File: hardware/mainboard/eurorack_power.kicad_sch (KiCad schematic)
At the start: 11 parts, among them J1 Eurorack PWR

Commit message: Add mixer circuitry
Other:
- moved on the sheet: C1, C2, C3, C4, D1, D2, D3, D4, J1, R1, R2

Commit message: Add footprints
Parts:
- C1, C2: footprint (none) -> Capacitor_SMD:CP_Elec_6.3x5.9
- C3, C4: footprint (none) -> Capacitor_SMD:C_0805_2012Metric_Pad1.18x1.45mm_HandSolder
- D1, D2: footprint (none) -> Diode_SMD:D_SOD-323F
- D3, D4: footprint (none) -> LED_SMD:LED_0805_2012Metric_Pad1.15x1.40mm_HandSolder
- J1: footprint (none) -> Connector_IDC:IDC-Header_2x05_P2.54mm_Latch6.5mm_Vertical
- R1, R2: footprint (none) -> Resistor_SMD:R_0805_2012Metric_Pad1.20x1.40mm_HandSolder

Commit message: Layout
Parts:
- J1: value Eurorack PWR -> Power Connector; footprint Connector_IDC:IDC-Header_2x05_P2.54mm_Latch6.5mm_Vertical -> Connector_IDC:IDC-Header_2x05_P2.54mm_Vertical
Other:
- moved on the sheet: C1, C2, C3, C4, D2

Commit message: Sent mainboard
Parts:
- C1, C2: LCSC_Part_No (none) -> C311666; Manufacturer (none) -> Lelon; Manufacturer_Part_No (none) -> OVK470M1ETR-0606
- C3, C4: LCSC_Part_No (none) -> C49678; Manufacturer (none) -> YAGEO; Manufacturer_Part_No (none) -> CC0805KRX7R9BB104
- D1, D2: LCSC_Part_No (none) -> C114696; Manufacturer (none) -> Nexperia; Manufacturer_Part_No (none) -> BAT46WJ,115
- D3, D4: LCSC_Part_No (none) -> C19171391; Manufacturer (none) -> YONGYUTAI; Manufacturer_Part_No (none) -> YLED0805R
- J1: LCSC_Part_No (none) -> C573025; Manufacturer (none) -> TE Connectivity; Manufacturer_Part_No (none) -> 1761681-3
- R1, R2: LCSC_Part_No (none) -> C17513; Manufacturer (none) -> UNI-ROYAL; Manufacturer_Part_No (none) -> 0805W8F1001T5E

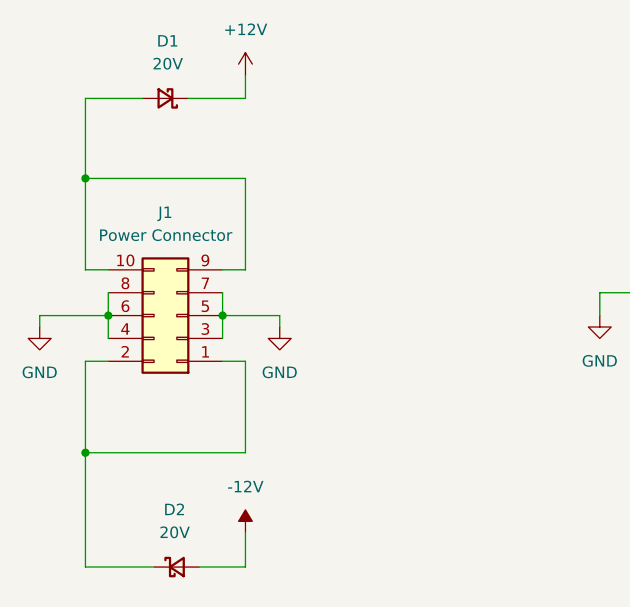
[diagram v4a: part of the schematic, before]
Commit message: Add 10Ω resistors to power rails
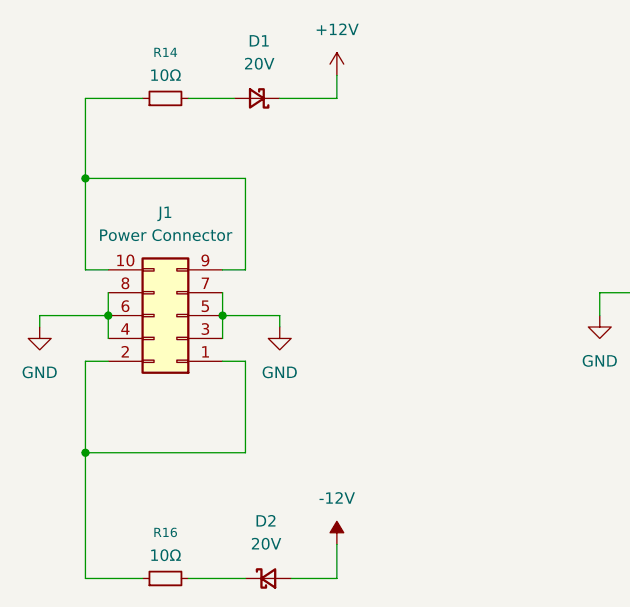
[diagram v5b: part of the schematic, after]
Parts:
- added R14, R16: 10Ω, Resistor_SMD:R_1206_3216Metric_Pad1.30x1.75mm_HandSolder, symbol Device:R_Small
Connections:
- net at J1.1 (Pin_1), J1.2 (Pin_2): now also R16.1; no longer D2.1 (K)
- net at J1.10 (Pin_10), J1.9 (Pin_9): now also R14.1; no longer D1.2 (A)
- new net: D2.1 (K), R16.2
- new net: D1.2 (A), R14.2
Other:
- moved on the sheet: D1, D2

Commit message: Updates
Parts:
- D1, D2: footprint Diode_SMD:D_SOD-323F -> EurorackFootprints:D_SOD-323F
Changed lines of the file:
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@@
 			)
 		)
-		(property "Footprint" "Diode_SMD:D_SOD-323F"
+		(property "Footprint" "EurorackFootprints:D_SOD-323F"
 			(at 86.36 107.95 90)
 			(effects
@@
 			)
 		)
-		(property "Footprint" "Diode_SMD:D_SOD-323F"
+		(property "Footprint" "EurorackFootprints:D_SOD-323F"
 			(at 85.09 54.61 90)
 			(effects
